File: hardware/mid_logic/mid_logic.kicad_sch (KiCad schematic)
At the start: 26 parts, among them J2 J_STK_A, J3 J_STK_B, J4 RS485 A/B/GND, J5 EXP P6/P7, Q2 BC847, SW1 RESET, SW2 BOOT, U1 ESP32-S3-WROOM-1-N16R8, U2 MAX3485, U3 PCF8574

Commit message: Reed-Kontakte, Haubenkontakt, Klinkenbuchse, ToF statt Radar
Funktional neu
--------------
- Zwei Reed-Eingaenge fuer Fensterkontakte auf den einzigen noch freien
  Expanderpins P6/P7. 10k Pullup, 1k Serie, 100n und TVS je Kanal; bei
  geschlossenem Kontakt liegen 0,3 V am PCF8574, sicher unter VIL.
- Meldekontakt zur Dunstabzugshaube ueber PhotoMOS AQY282GS statt Relais:
  potentialfrei, 60 V / 0,8 A, kein Spulenstrom, keine Bauhoehe im 9-mm-
  Stapelspalt. NUR SELV - bei 230 V gehoert das Schaltglied nicht in die Dose.
- Weihnachtsstern jetzt gesteckt: Klinkenbuchse im oberen Steg der
  Frontplatte, PTC 0,2 A direkt an der Buchse gegen den Kurzschluss beim
  Stecken, Bulk vor die Sicherung gelegt.
- Radar durch VL53L1X (ToF) ersetzt. Hinter dieser Frontplatte hat kein
  20-mm-Radarmodul freie Sicht; der ToF passt als 4,9 x 2,5 mm grosser Chip
  in den Steg. Er misst Entfernung statt Empfindlichkeit - Schwelle exakt
  1 m - und deckt in der Fensterlaibung zugleich den Durchstieg ab.
  Netze umbenannt: RADAR_INT -> PRESENCE_INT, UART_RADAR_* -> UART_AUX_*.
  J7 bleibt unbestueckt als Reserve, damit das Stackpinout unberuehrt bleibt.

Frontplatte
-----------
Oberer Steg 9 -> 17 mm, damit Klinkenbuchse und ToF-Fenster nebeneinander
passen; Sicheln dadurch ~70 -> ~45 Grad, Stoesselwinkel 18 -> 12 Grad.
ToF-Kanal konisch (4,5 vorn, 3,0 hinten) fuer den Sichtkegel. Kabelausgang
Ø4,5 entfaellt. Selbsttests bestanden, STEP/STL neu erzeugt.

KiCad 10
--------
Die Generatoren liefen nur gegen KiCad-9-Bibliotheken. Migriert:
- Symbol- und Footprintpfad werden gefunden (Linux, macOS, Umgebungsvariable)
- PCF8574 -> PCF8574T (pinkompatibel, als Alias)
- Q_NMOS_GDS/Q_PMOS_GSD/Q_NPN_BCE liegen jetzt als hardware/lib/
  SwitchStack.kicad_sym im Projekt. KiCad 10 nummeriert die Stockvarianten
  mit G/D/S bzw. B/C/E - ein Alias haette die Anschluesse still vertauscht.
- USB-C-Schirm heisst SH statt S1, Zonen-API SetDoNotAllowZoneFills,
  DRC laeuft ueber kicad-cli statt WriteDRCRepo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
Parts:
- added C7, C8: 100n, Capacitor_SMD:C_0603_1608Metric, symbol Device:C
- added D2, D3: 5V6, Diode_SMD:D_SOD-123, symbol Device:D_TVS
- added D4: 33V, Diode_SMD:D_SOD-123, symbol Device:D_TVS
- added R10, R9: 10k, Resistor_SMD:R_0603_1608Metric, symbol Device:R
- added R11, R12: 1k, Resistor_SMD:R_0603_1608Metric, symbol Device:R
- added R13: 330R, Resistor_SMD:R_0603_1608Metric, symbol Device:R
- added U4: PhotoMOS 60V, Package_SO:SOP-4_4.4x2.6mm_P1.27mm, symbol Relay_SolidState:AQY282GS
- J5: value EXP P6/P7 -> Feld: Reed 1/2, Haube; footprint Connector_PinHeader_2.54mm:PinHeader_1x02_P2.54mm_Vertical -> Connector_JST:JST_SH_BM06B-SRSS-TB_1x06-1MP_P1.00mm_Vertical; symbol Connector_Generic:Conn_01x02 -> Connector_Generic:Conn_01x06; MPN (none) -> 1 REED1 2 GND 3 REED2 4 GND 5 HAUBE_A 6 HAUBE_B
- Q2: symbol Device:Q_NPN_BCE -> SwitchStack:Q_NPN_BCE
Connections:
- net 3V3_SYS: now also J5.2 (Pin_2), J5.4 (Pin_4), C7.2, C8.2, D2.2 (A2), D3.2 (A2), R10.1, R13.1, R9.1
- net EXP_P6: now also C7.1, R11.2, R9.2; no longer J5.1 (Pin_1)
- net EXP_P7: now also C8.1, R10.2, R12.2; no longer J5.2 (Pin_2)
- net RELAY_CTL: now also U4.2
- net RADAR_INT renamed PRESENCE_INT
- net UART_RADAR_RX renamed UART_AUX_RX
- net UART_RADAR_TX renamed UART_AUX_TX
- new net HOOD_A: D4.1 (A1), J5.5 (Pin_5), U4.4
- new net HOOD_B: D4.2 (A2), J5.6 (Pin_6), U4.3
- new net REED1_IN: D2.1 (A1), J5.1 (Pin_1), R11.1
- new net REED2_IN: D3.1 (A1), J5.3 (Pin_3), R12.1
- new net RELAY_LED: R13.2, U4.1
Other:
- moved on the sheet: BZ1, D1, J2, J3, Q2, R8

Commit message: Drei Entscheidungen umgesetzt: 9 A, vier Reed-Kontakte, einstellbare Fahrzeiten
Beide Motoren duerfen gleichzeitig laufen (Punkt 3)
---------------------------------------------------
Kein Interlock. Damit gilt der Summenpfad von 9 A - also genau die Auslegung,
die Sicherung, Leiterbahnen und Steckverbinder ohnehin schon zugrunde legen.
Die Entscheidung kostet nichts, weil defensiv gerechnet wurde. Sie verschaerft
aber Punkt 2: Der Hochstrom-Steckverbinder muss die 9 A wirklich koennen, ein
Rueckzug auf 4,9 A ist nicht mehr moeglich.

Vier Reed-Kontakte (Punkt 34)
-----------------------------
Die Sabotageueberwachung bleibt, zwei Kontakte je Fenster. Umgesetzt ueber
einen PCF8575 statt des PCF8574: gleiche Adresse, gleicher Treiber, ein Bauteil
statt zwei. Verschluss auf P6/P7, Sabotage auf P10/P11 (ESPHome 8/9), P12-P17
Reserve. Vier gleiche Eingangsnetzwerke, 10k Pullup + 1k Serie + 100n + TVS.

Das Mid-Board war damit voll - buchstaeblich. Zwei Zwaenge liessen sich nur
gemeinsam loesen:

  * Der 8-polige Feldstecker (11,9 mm) findet keinen Platz. Zwei kleinere
    finden beide einen: J5 sechspolig fuer die vier Reed-Signale, J6 zweipolig
    fuer den Haubenkontakt. Das trennt nebenbei Eingaenge und Schaltausgang.
  * Der PCF8575 im SSOP-24 fand auf dem ganzen Board keine Stelle, solange der
    Piezo ein THT-Teil war - der blockierte mit 12,5 x 12,6 mm BEIDE Seiten.
    Mit einem SMD-Wandler (Murata PKMCS0909E, 9 x 9 x 3) geht der Expander auf
    die Rueckseite. Das war genau der Hebel, den Punkt 29 dafuer vorgesehen
    hatte. Preis: Ein 9-mm-SMD-Wandler ist leiser als ein 12-mm-THT-Typ; ob er
    hinter der zugeschraubten Blende reicht, ist zu pruefen (Punkt 22).

Mid steht jetzt bei 46 Bauteilen, Platzierung kollisionsfrei, DRC ohne Fehler.

Einstellbare Fahrzeiten und Stromskalierung
-------------------------------------------
Die Jalousien laufen nicht mehr als time_based-Cover - deren Dauer steht zur
Compilezeit fest. Stattdessen template-Cover mit Fahrsk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
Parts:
- added C10, C9: 100n, Capacitor_SMD:C_0603_1608Metric, symbol Device:C
- added D5, D6: 5V6, Diode_SMD:D_SOD-123, symbol Device:D_TVS
- added J6: Haubenkontakt, Connector_JST:JST_SH_BM02B-SRSS-TB_1x02-1MP_P1.00mm_Vertical, symbol Connector_Generic:Conn_01x02
- added R14, R15: 10k, Resistor_SMD:R_0603_1608Metric, symbol Device:R
- added R16, R17: 1k, Resistor_SMD:R_0603_1608Metric, symbol Device:R
- BZ1: value Piezo passiv -> Piezo passiv SMD; footprint Buzzer_Beeper:Buzzer_12x9.5RM7.6 -> Buzzer_Beeper:Buzzer_Murata_PKMCS0909E; MPN passiv - aktiver Summer kann keine rtttl-Melodien -> Murata PKMCS0909E o.ae., 9 x 9 x 3 mm SMD - passiv, ein akt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
- J5: value Feld: Reed 1/2, Haube -> Feld: 4 Reed; MPN 1 REED1 2 GND 3 REED2 4 GND 5 HAUBE_A 6 HAUBE_B -> 1 REED1 2 SAB1 3 GND | 4 REED2 5 SAB2 6 GND
- U3: value PCF8574 -> PCF8575; footprint Package_SO:SOIC-16_3.9x9.9mm_P1.27mm -> Package_SO:SSOP-24_5.3x8.2mm_P0.65mm; symbol Interface_Expansion:PCF8574 -> Interface_Expansion:PCF8575DBR
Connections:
- net 3V3_SYS: now also J5.3 (Pin_3), J5.6 (Pin_6), U3.12 (GND), U3.21 (A0), U3.24 (VCC), C10.2, C9.2, D5.2 (A2), D6.2 (A2), R14.1, R15.1; no longer J5.2 (Pin_2), J5.4 (Pin_4), U3.1 (A0), U3.16 (VDD), U3.8 (GND)
- net EXP_P6: now also U3.10 (P6); no longer U3.11 (P6)
- net EXP_P7: now also U3.11 (P7); no longer U3.12 (P7)
- net HOOD_A: now also J6.1 (Pin_1); no longer J5.5 (Pin_5)
- net HOOD_B: now also J6.2 (Pin_2); no longer J5.6 (Pin_6)
- net I2C_SCL: now also U3.22 (SCL); no longer U3.14 (SCL)
- net I2C_SDA: now also U3.23 (SDA); no longer U3.15 (SDA)
- net PRESENCE_INT: now also U3.8 (P4); no longer U3.9 (P4)
- net REED2_IN: now also J5.4 (Pin_4); no longer J5.3 (Pin_3)
- net RELAY_CTL: now also U3.9 (P5); no longer U3.10 (P5)
- net EXP_P8: now reaches U3.13 (P10)
- net EXP_P8: now also C9.1, R14.2, R16.2
- new net EXP_P9: C10.1, R15.2, R17.2, U3.14 (P11)
- new net SAB1_IN: D5.1 (A1), J5.2 (Pin_2), R16.1
- new net SAB2_IN: D6.1 (A1), J5.5 (Pin_5), R17.1
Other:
- moved on the sheet: BZ1, D1, D4, J2, J3, J5, Q2, R13, R8, U4

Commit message: USB-C wandert auf das Mid-Board, Top bekommt eine Randkerbe
Der Grund ist Bauhoehe, nicht Routing. Ueber dem Top-Board sind bis zur
Zentralscheibe 3,5 mm frei; eine stehende USB-C-Buchse baut 7 bis 9,25 mm
(GCT USB4115: H = 9,25 mm laut Datenblatt). Sie haette die Scheibe
durchstossen. Zwischen Mids und Tops Oberseite liegen dagegen 10,0 mm.

Die Buchse steht jetzt auf Mid bei (3,5 / 20,3) und greift durch eine offene
Randkerbe des Top-Boards nach vorn - gesteckt wird weiterhin frontal, sobald
die Zentralscheibe ab ist. Koerper 8,3 x 4,3 mm, Kerbe 11,0 mm breit ab
y = 16,8 bis zum Rand.

Offene Kerbe statt Fenster, weil der Boardrand bei y = 23,5 liegt: Ein
geschlossenes Fenster liesse einen Steg von einem halben Millimeter stehen,
der beim Nutzentrennen bricht.

MITGEWANDERT sind die ESD-Diode (U5) und die beiden CC-Widerstaende
(R18/R19). Damit verlieren USB_DP und USB_DN ihren Weg durch den Stapel:
J_STK_A 34/36 heissen jetzt RSV_A3/RSV_A5. Der native USB des ESP32-S3 sitzt
auf demselben Board wie die Buchse. Stack-Pinout auf v0.4.

USB_VBUS bleibt auf A18 - es geht weiter nach unten zum Power-Mux auf Bottom,
kommt jetzt nur von Mid statt von Top.

PLATZIERUNG. Der Bodenrand von Mid war belegt: RS485 (J4) nach links auf
(-11,5 / 19,0) gerueckt, PhotoMOS (U4) aus der Fixliste genommen. Ein
Rastersuchlauf ueber beide Seiten fand fuer U4 keine freie Flaeche von
11,6 x 3,6 mm - der automatische Platzierer bringt ihn jetzt selbst unter und
hat ihn nach (-20,1 / 7,9) gelegt. Oben ging es nicht, dort steht das
ESP32-Modul mit seiner Antenne; links und rechts laesst Tops Displayfenster
nur 7,2 mm Rand.

inside_outline() kennt die Kerbe, der Platzierer legt dort nichts ab, und der
Zonenumriss folgt ihr.

  top_ui     27 -> 21 Bauteile, unrouted 63 -> 48
  mid_logic  46 -> 50 Bauteile

Co-Authored-By: Claude Opus 5 (1M context) <noreply@anthropic.com>
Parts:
- added J7: USB-C, Connector_USB:USB_C_Receptacle_G-Switch_GT-USB-7051x, symbol Connector:USB_C_Receptacle_USB2.0_16P
- added R18, R19: 5k1, Resistor_SMD:R_0603_1608Metric, symbol Device:R
- added U5: USBLC6-2SC6, Package_TO_SOT_SMD:SOT-23-6, symbol Power_Protection:USBLC6-2SC6
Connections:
- net 3V3_SYS: no longer C1.2, C10.2, C2.2, C3.2, C4.2, C5.2, C6.2, C7.2, C8.2, C9.2, D2.2 (A2), D3.2 (A2), D5.2 (A2), D6.2 (A2), J2.1 (Pin_1), J2.11 (Pin_11), J2.12 (Pin_12), J2.14 (Pin_14), J2.15 (Pin_15), J2.19 (Pin_19), J2.2 (Pin_2), J2.21 (Pin_21), J2.25 (Pin_25), J2.38 (Pin_38), J2.39 (Pin_39), J2.40 (Pin_40), J2.7 (Pin_7), J2.8 (Pin_8), J3.1 (Pin_1), J3.11 (Pin_11), J3.13 (Pin_13), J3.17 (Pin_17), J3.19 (Pin_19), J3.2 (Pin_2), J3.22 (Pin_22), J3.25 (Pin_25), J3.30 (Pin_30), J3.33 (Pin_33), J3.39 (Pin_39), J3.40 (Pin_40), J3.5 (Pin_5), J3.7 (Pin_7), J3.9 (Pin_9), J4.3 (Pin_3), J5.3 (Pin_3), J5.6 (Pin_6), Q2.3 (E), R4.2, SW1.2, SW2.2, U1.1 (GND), U1.40 (GND), U1.41 (GND), U2.5 (GND), U3.12 (GND), U3.2 (A1), U3.21 (A0), U3.3 (A2)
- net USB_DN: now also U5.6 (I/O1); no longer J2.36 (Pin_36)
- net USB_DP: now also U5.4 (I/O2); no longer J2.34 (Pin_34)
- net USB_VBUS: now also J7.A4 (VBUS), J7.A9 (VBUS), J7.B4 (VBUS), J7.B9 (VBUS), U5.5 (VBUS)
- new net PGND: C1.2, C10.2, C2.2, C3.2, C4.2, C5.2, C6.2, C7.2, C8.2, C9.2, D2.2 (A2), D3.2 (A2), D5.2 (A2), D6.2 (A2), J2.1 (Pin_1), J2.11 (Pin_11), J2.12 (Pin_12), J2.14 (Pin_14), J2.15 (Pin_15), J2.19 (Pin_19), J2.2 (Pin_2), J2.21 (Pin_21), J2.25 (Pin_25), J2.38 (Pin_38), J2.39 (Pin_39), J2.40 (Pin_40), J2.7 (Pin_7), J2.8 (Pin_8), J3.1 (Pin_1), J3.11 (Pin_11), J3.13 (Pin_13), J3.17 (Pin_17), J3.19 (Pin_19), J3.2 (Pin_2), J3.22 (Pin_22), J3.25 (Pin_25), J3.30 (Pin_30), J3.33 (Pin_33), J3.39 (Pin_39), J3.40 (Pin_40), J3.5 (Pin_5), J3.7 (Pin_7), J3.9 (Pin_9), J4.3 (Pin_3), J5.3 (Pin_3), J5.6 (Pin_6), J7.A1 (GND), J7.A12 (GND), J7.B1 (GND), J7.B12 (GND), J7.SH (SHIELD), Q2.3 (E), R18.2, R19.2, R4.2, SW1.2, SW2.2, U1.1 (GND), U1.40 (GND), U1.41 (GND), U2.5 (GND), U3.12 (GND), U3.2 (A1), U3.21 (A0), U3.3 (A2), U5.2 (GND)
- new net RSV_A3: J2.34 (Pin_34)
- new net RSV_A5: J2.36 (Pin_36)
- new net USB_CC1: J7.A5 (CC1), R18.1
- new net USB_CC2: J7.B5 (CC2), R19.1
- new net USB_DN_C: J7.A7 (D-), J7.B7 (D-), U5.1 (I/O1)
- new net USB_DP_C: J7.A6 (D+), J7.B6 (D+), U5.3 (I/O2)
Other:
- moved on the sheet: BZ1, C1, C10, C2, C3, C4, C5, C6, C7, C8, C9, D1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

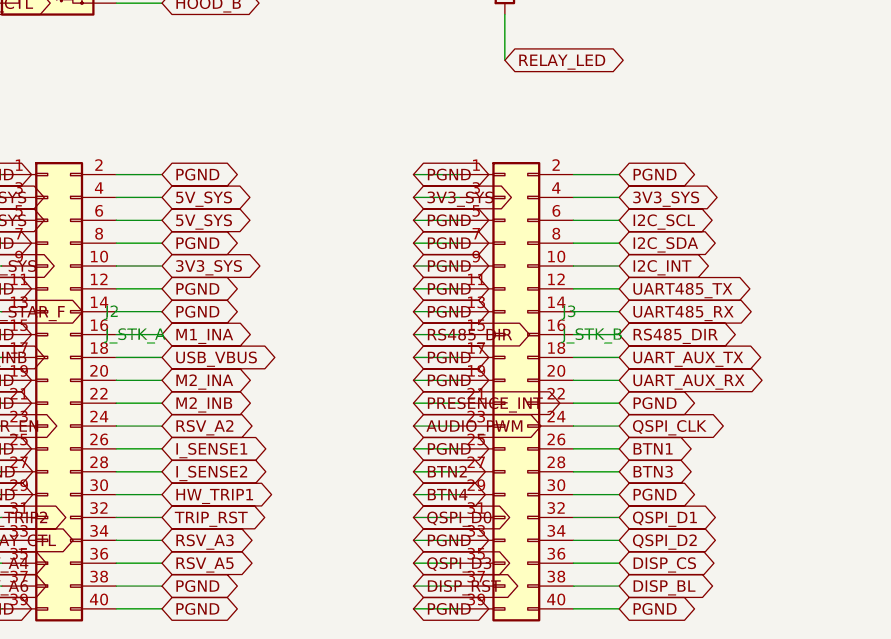
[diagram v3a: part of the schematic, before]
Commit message: Stack-Pinout v0.5: Tasten und I2C auf die Aussenreihe, Tasten auf beide Verbinder
Zwei Autorouter (1.9.0 und 2.3.0) und zwei Lagenzahlen hatten auf Top exakt
dieselben elf offenen Netze hinterlassen. Das ist kein Werkzeugproblem,
sondern die Pinbelegung.

BTN1..BTN4 lagen auf B26..B29 - vier benachbarten Kontakten der INNENreihe
des RECHTEN Verbinders. Ihre Taster sitzen aber in allen vier Ecken des
Top-Boards, zwei davon links. Zwei Bahnen mussten quer ueber ein Board mit
80 Steckkontakten im 1,27-mm-Raster, und alle vier zuerst aus der Innenreihe
heraus. I2C_SCL/SDA lagen ebenfalls innen.

Neu liegt jedes Tastennetz auf der AUSSENreihe des Verbinders, der seiner
Ecke am naechsten ist - von dort geht es direkt nach aussen und am Boardrand
entlang zum Taster:

  BTN1  B26 -> B1    aussen, y = -14,06   SW1 (+18 / -20)
  BTN2  B27 -> A2    aussen, y = -14,06   SW2 (-18 / -20)
  BTN3  B28 -> A40   aussen, y = +10,07   SW3 (-18 / +20)
  BTN4  B29 -> B39   aussen, y = +10,07   SW4 (+18 / +20)

  I2C_SCL  B6 -> B5  aussen
  I2C_SDA  B8 -> B7  aussen

Beide I2C-Teilnehmer auf Top - SHT4x und ToF - sitzen an der oberen Kante,
also dort, wo die neuen Pins liegen.

Die freigewordenen Kontakte B6, B8, B26..B29 werden PGND. Vier PGND-Pins sind
weggefallen (A2, A40, B1, B39); ueber beide Verbinder bleiben 25.

Alle drei Schaltplaene und Layouts neu erzeugt, Netzlistenvergleich bestanden,
keine Platzierungsfehler. Das Routing folgt.

Co-Authored-By: Claude Opus 5 (1M context) <noreply@anthropic.com>
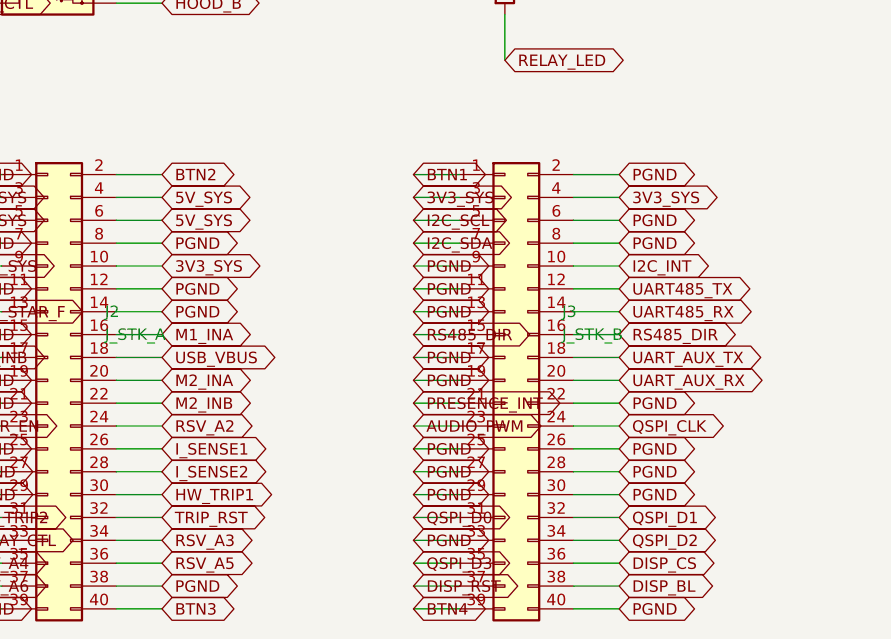
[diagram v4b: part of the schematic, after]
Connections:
- net BTN1: now also J3.1 (Pin_1); no longer J3.26 (Pin_26)
- net BTN2: now also J2.2 (Pin_2); no longer J3.27 (Pin_27)
- net BTN3: now also J2.40 (Pin_40); no longer J3.28 (Pin_28)
- net BTN4: now also J3.39 (Pin_39); no longer J3.29 (Pin_29)
- net I2C_SCL: now also J3.5 (Pin_5); no longer J3.6 (Pin_6)
- net I2C_SDA: now also J3.7 (Pin_7); no longer J3.8 (Pin_8)
- net PGND: now also J3.26 (Pin_26), J3.27 (Pin_27), J3.28 (Pin_28), J3.29 (Pin_29), J3.6 (Pin_6), J3.8 (Pin_8); no longer J2.2 (Pin_2), J2.40 (Pin_40), J3.1 (Pin_1), J3.39 (Pin_39), J3.5 (Pin_5), J3.7 (Pin_7)

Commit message: docs/16: Anleitung fuer die letzten Handgriffe in KiCad
Was der Autorouter uebrig laesst, ist wenig und immer dasselbe Muster: Pads,
die zwischen anderen Bauteilen eingeklemmt sind. Die Anleitung nennt die
Tastenkuerzel (X fuer Bahn, V fuer Lagenwechsel mit Via, B fuer Zonen
fuellen), den aktuellen Stand je Board als Anhaltspunkt und die
Reihenfolge danach - Zonen fuellen VOR der DRC, sonst sucht man Fehler, die
keine sind.

Dazu zwei Warnungen: keine Bauteile verschieben, die Positionen kommen aus
gen_layouts.py und gehen beim naechsten Neuerzeugen verloren. Und die Regeln
nicht lockern - wenn die DRC meckert, ist die Bahn falsch.

Co-Authored-By: Claude Opus 5 (1M context) <noreply@anthropic.com>
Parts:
- removed J4: RS485 A/B/GND, Connector_JST:JST_XH_B3B-XH-A_1x03_P2.50mm_Vertical, symbol Connector_Generic:Conn_01x03
- removed J5: Feld: 4 Reed, Connector_JST:JST_SH_BM06B-SRSS-TB_1x06-1MP_P1.00mm_Vertical, symbol Connector_Generic:Conn_01x06
- removed J6: Haubenkontakt, Connector_JST:JST_SH_BM02B-SRSS-TB_1x02-1MP_P1.00mm_Vertical, symbol Connector_Generic:Conn_01x02
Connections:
- net RSV_A2 is gone; now on net REED2_IN: J2.24 (Pin_24)
- net RSV_A3 is gone; now on net RS485_A: J2.34 (Pin_34)
- net RSV_A4 is gone; now on net RS485_B: J2.35 (Pin_35)
- net RSV_A5 is gone; now on net REED1_IN: J2.36 (Pin_36)
- net RSV_A6 is gone; now on net SAB1_IN: J2.37 (Pin_37)
- net HOOD_A: now also J2.38 (Pin_38)
- net HOOD_B: now also J2.39 (Pin_39)
- net PGND: no longer J2.25 (Pin_25), J2.38 (Pin_38), J2.39 (Pin_39)
- net SAB2_IN: now also J2.25 (Pin_25)
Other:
- moved on the sheet: BZ1, C10, C6, C7, C8, C9, D1, D2, D3, D4, D5, D6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

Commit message: Punkt 23 im Layout: Mid traegt den Durchsteck-Stift, mit dem Lochbild der Buchse
Seit dem Beschluss (C43383 auf Mid, C41370657 auf Bottom und Top) sass im
Layout auf allen drei Boards noch die Buchse. Der naheliegende Tausch auf
KiCads PinHeader_2x20_P1.27mm_Vertical geht nicht: Der Header hat Reihe 2
bei +1,27, die Buchse bei -1,27. Ein Tausch haette 40 Bohrungen um 2,54 mm
verschoben und jede Bahn dorthin abgerissen - und gesteckt haette es auch
nicht mehr, weil die Stifte in die Buchsen der Nachbarn muessen, also auf
DEREN Lochbild.

Deshalb ein projektlokaler Footprint SwitchStack:PinHeader_2x20_P1.27mm_
Vertical_Durchsteck: Pads und Bohrung (0,7) wie die Buchse, Beschreibung
sagt warum, 3D-Modell des KiCad-Headers um 180 Grad gedreht und um eine
Reihenlaenge verschoben (3D-y zeigt gegen Board-y, deshalb -24,13) und um
1,45 mm angehoben - so wird er geloetet, mit Unterlage, damit der Pin
beidseitig 3,05 uebersteht. Im Render sitzt er auf den Pads.

J2 und J3 im Layout per pcbnew getauscht: Position, Lage, Referenz, Wert
und das versteckte LCSC-Feld uebernommen, alle 40 Netze je Stecker Pad
fuer Pad geprueft. DRC unveraendert (offen 15, Kupferfehler 0).

Damit es das Regenerieren ueberlebt: gen_mid_sch uebergibt den Footprint an
connect_stack, der Mid-Schaltplan traegt ihn, lcsc_nachtragen sucht auf Mid
nach PinHeader_2x20 statt PinSocket_2x20. docs/16: nicht anfassen.

Co-Authored-By: Claude Fable 5.1 <noreply@anthropic.com>
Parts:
- J2, J3: footprint Connector_PinSocket_1.27mm:PinSocket_2x20_P1.27mm_Vertical -> SwitchStack:PinHeader_2x20_P1.27mm_Vertical_Durchsteck
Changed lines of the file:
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@@
     (property "Value" "J_STK_A" (at 31.7500 242.5700 0)
       (effects (font (size 1.27 1.27)) (justify left)))
-    (property "Footprint" "Connector_PinSocket_1.27mm:PinSocket_2x20_P1.27mm_Vertical" (at 25.4000 247.6500 0)
+    (property "Footprint" "SwitchStack:PinHeader_2x20_P1.27mm_Vertical_Durchsteck" (at 25.4000 247.6500 0)
       (effects (font (size 1.27 1.27)) hide))
     (pin "1")
@@
     (property "Value" "J_STK_B" (at 82.5500 242.5700 0)
       (effects (font (size 1.27 1.27)) (justify left)))
-    (property "Footprint" "Connector_PinSocket_1.27mm:PinSocket_2x20_P1.27mm_Vertical" (at 76.2000 247.6500 0)
+    (property "Footprint" "SwitchStack:PinHeader_2x20_P1.27mm_Vertical_Durchsteck" (at 76.2000 247.6500 0)
       (effects (font (size 1.27 1.27)) hide))
     (pin "1")
